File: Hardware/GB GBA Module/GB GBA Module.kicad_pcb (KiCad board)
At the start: 2 copper layers, 125 x 119 mm, 11 parts, among them J1 Conn_01x32, J2 Conn_01x31_Pin, J3 Conn_01x32, J4 Conn_01x31_Pin

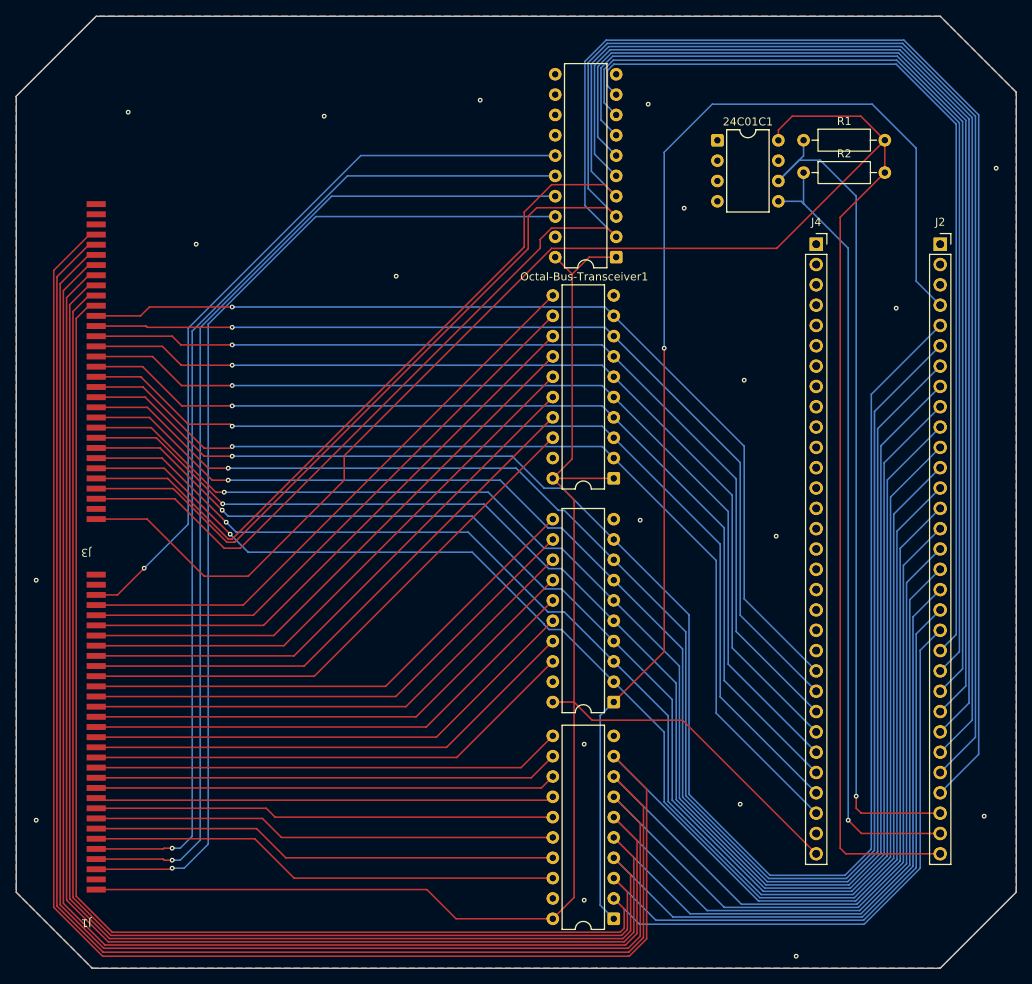
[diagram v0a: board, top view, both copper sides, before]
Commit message: Updated Final Report, Added NES Arduino Code
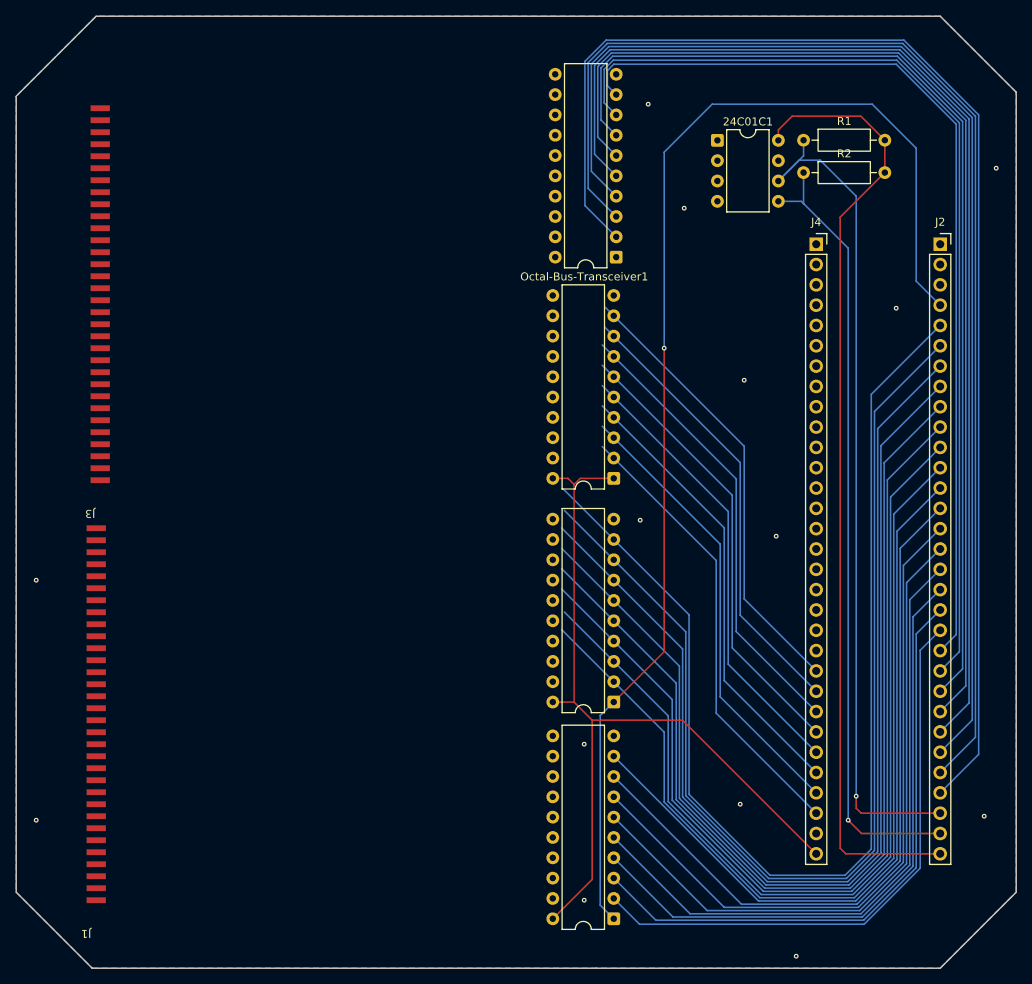
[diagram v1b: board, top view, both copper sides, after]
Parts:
- moved J3 4.89 mm to (99.3, 84.7)
- moved J1 1.33 mm to (98.8, 137.2)
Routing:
- net Net-(J2-Pin_13): track 282.6 -> 93.7 mm
- net Net-(J2-Pin_14): track 274.1 -> 90.8 mm
- net Net-(J2-Pin_15): track 265.7 -> 87.9 mm
- net Net-(J2-Pin_16): track 257.2 -> 84.9 mm
- net Net-(J2-Pin_17): track 248.6 -> 82.0 mm
- net Net-(J2-Pin_18): track 240.2 -> 79.1 mm
- net Net-(J2-Pin_19): track 231.8 -> 76.2 mm
- net Net-(J2-Pin_20): track 223.5 -> 73.3 mm
- net Net-(J1-Pin_4): track 129.3 -> 0.00 mm, vias 1 -> 0
- net Net-(J1-Pin_3): track 129.3 -> 0.00 mm, vias 1 -> 0
- net Net-(J1-Pin_5): track 129.2 -> 0.00 mm, vias 1 -> 0
- net Net-(24C01C1-VCC): track 246.1 -> 120.2 mm
- net Net-(J1-Pin_1): track 200.1 -> 103.1 mm
- net Net-(J1-Pin_30): track 94.5 -> 0.00 mm, vias 1 -> 0
- net Net-(J2-Pin_26): track 240.6 -> 151.0 mm
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
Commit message: Commented Code, Converted documents to PDF.
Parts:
- moved Octal-Bus-Transceiver1 0.39 mm to (164.6, 53.2)
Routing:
- net Net-(24C01C1-VCC): track 120.2 -> 280.2 mm
- net Net-(J1-Pin_3): track 0.00 -> 132.8 mm
- net Net-(J1-Pin_4): track 0.00 -> 129.1 mm
- net Net-(J1-Pin_5): track 0.00 -> 124.6 mm
- net Net-(J2-Pin_20): track 73.3 -> 188.9 mm, vias 0 -> 2
- net Net-(J2-Pin_19): track 76.2 -> 190.3 mm, vias 0 -> 2
- net Net-(J2-Pin_18): track 79.1 -> 192.6 mm, vias 0 -> 2
- net Net-(J2-Pin_17): track 82.0 -> 193.8 mm, vias 0 -> 2
- net Net-(J2-Pin_16): track 84.9 -> 195.5 mm, vias 0 -> 2
- net Net-(J2-Pin_15): track 87.9 -> 197.7 mm, vias 0 -> 2
- net Net-(J2-Pin_14): track 90.8 -> 200.5 mm, vias 0 -> 2
- net Net-(J2-Pin_13): track 93.7 -> 199.2 mm, vias 0 -> 2
- net Net-(J2-Pin_26): track 151.0 -> 234.1 mm, vias 0 -> 1
- net Net-(J2-Pin_27): track 157.7 -> 237.6 mm, vias 0 -> 1
- net Net-(J1-Pin_30): track 0.00 -> 77.9 mm
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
